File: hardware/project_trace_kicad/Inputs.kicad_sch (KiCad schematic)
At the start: 41 parts, among them J201 Conn_01x01_Socket, J202 Conn_01x01_Socket, J203 Conn_01x01_Socket, J204 Screw_Terminal_01x04, J205 Conn_Coaxial, U1 OPA2837IRUNT, U2 OPA2837IRUNT, U202 AQW280SX, U203 AQW282SX, U204 TS5A23159DGS, U206 TLE2426xLP

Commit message: Fix Footprints, Add ADC Footpring, begin Layout
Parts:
- U1, U2: footprint (none) -> ProjectTraceFootprints:OPA2837IRUNT; DigikeyPN (none) -> 296-53042-1-ND
- U204: footprint Package_SO:VSSOP-10_3x3mm_P0.5mm -> ProjectTraceFootprints:SOIC-10 - DGS0010A
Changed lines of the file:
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@@
 			)
 		)
-		(property "Footprint" "Package_SO:VSSOP-10_3x3mm_P0.5mm"
+		(property "Footprint" "ProjectTraceFootprints:SOIC-10 - DGS0010A"
 			(at 196.85 95.885 0)
 			(hide yes)
@@
 			)
 		)
-		(property "Footprint" ""
+		(property "Footprint" "ProjectTraceFootprints:OPA2837IRUNT"
 			(at 157.48 142.24 0)
 			(hide yes)
@@
 			)
 		)
+		(property "DigikeyPN" "296-53042-1-ND"
+			(at 157.48 142.24 0)
+			(hide yes)
+			(show_name no)
+			(do_not_autoplace no)
+			(effects
+				(font
+					(size 1.27 1.27)
+				)
+			)
+		)
 		(pin "10"
 		)
@@
 			)
 		)
-		(property "Footprint" ""
+		(property "Footprint" "ProjectTraceFootprints:OPA2837IRUNT"
 			(at 123.19 63.5 0)
 			(hide yes)
@@
 			)
 		)
+		(property "DigikeyPN" "296-53042-1-ND"
+			(at 123.19 63.5 0)
+			(hide yes)
+			(show_name no)
+			(do_not_autoplace no)
+			(effects
+				(font
+					(size 1.27 1.27)
+				)
+			)
+		)
 		(pin "6"
 		)
@@
 			)
 		)
-		(property "Footprint" ""
+		(property "Footprint" "ProjectTraceFootprints:OPA2837IRUNT"
 			(at 123.19 36.83 0)
 			(hide yes)
@@
 			)
 		)
+		(property "DigikeyPN" "296-53042-1-ND"
+			(at 123.19 36.83 0)
+			(hide yes)
+			(show_name no)
+			(do_not_autoplace no)
+			(effects
+				(font
+					(size 1.27 1.27)
+				)
+			)
+		)
 		(pin "6"
 		)
@@
 			)
 		)
-		(property "Footprint" ""
+		(property "Footprint" "ProjectTraceFootprints:OPA2837IRUNT"
 			(at 245.11 66.04 0)
 			(hide yes)
@@
 			)
 		)
+		(property "DigikeyPN" "296-53042-1-ND"
+			(at 245.11 66.04 0)
+			(hide yes)
+			(show_name no)
+			(do_not_autoplace no)
+			(effects
+				(font
+					(size 1.27 1.27)
+				)
+			)
+		)
 		(pin "10"
 		)
@@
 			)
 		)
-		(property "Footprint" "Package_SO:VSSOP-10_3x3mm_P0.5mm"
+		(property "Footprint" "ProjectTraceFootprints:SOIC-10 - DGS0010A"
 			(at 158.75 73.025 0)
 			(hide yes)
@@
 			)
 		)
-		(property "Footprint" ""
+		(property "Footprint" "ProjectTraceFootprints:OPA2837IRUNT"
 			(at 189.23 63.5 0)
 			(hide yes)
@@
 			)
 		)
+		(property "DigikeyPN" "296-53042-1-ND"
+			(at 189.23 63.5 0)
+			(hide yes)
+			(show_name no)
+			(do_not_autoplace no)
+			(effects
+				(font
+					(size 1.27 1.27)
+				)
+			)
+		)
 		(pin "10"
 		)
@@
 			)
 		)
-		(property "Footprint" "Package_SO:VSSOP-10_3x3mm_P0.5mm"
+		(property "Footprint" "ProjectTraceFootprints:SOIC-10 - DGS0010A"
 			(at 252.73 158.115 0)
 			(hide yes)
@@
 			)
 		)
-		(property "Footprint" ""
+		(property "Footprint" "ProjectTraceFootprints:OPA2837IRUNT"
 			(at 191.77 142.24 0)
 			(hide yes)
@@
 			(at 191.77 142.24 0)
 			(hide yes)
+			(show_name no)
+			(do_not_autoplace no)
+			(effects
+				(font
+					(size 1.27 1.27)
+				)
+			)
+		)
+		(property "DigikeyPN" "296-53042-1-ND"
+			(at 191.77 142.24 0)
+			(hide yes)

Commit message: Update Inputs.kicad_sch
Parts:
- U1, U2: footprint ProjectTraceFootprints:OPA2837IRUNT -> ProjectTraceFootprints:OPA2837IRUNT-Handsolder
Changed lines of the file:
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@@
 			)
 		)
-		(property "Footprint" "ProjectTraceFootprints:OPA2837IRUNT"
+		(property "Footprint" "ProjectTraceFootprints:OPA2837IRUNT-Handsolder"
 			(at 157.48 142.24 0)
 			(hide yes)
@@
 			)
 		)
-		(property "Footprint" "ProjectTraceFootprints:OPA2837IRUNT"
+		(property "Footprint" "ProjectTraceFootprints:OPA2837IRUNT-Handsolder"
 			(at 123.19 63.5 0)
 			(hide yes)
@@
 			)
 		)
-		(property "Footprint" "ProjectTraceFootprints:OPA2837IRUNT"
+		(property "Footprint" "ProjectTraceFootprints:OPA2837IRUNT-Handsolder"
 			(at 123.19 36.83 0)
 			(hide yes)
@@
 			)
 		)
-		(property "Footprint" "ProjectTraceFootprints:OPA2837IRUNT"
+		(property "Footprint" "ProjectTraceFootprints:OPA2837IRUNT-Handsolder"
 			(at 245.11 66.04 0)
 			(hide yes)
@@
 			)
 		)
-		(property "Footprint" "ProjectTraceFootprints:OPA2837IRUNT"
+		(property "Footprint" "ProjectTraceFootprints:OPA2837IRUNT-Handsolder"
 			(at 189.23 63.5 0)
 			(hide yes)
@@
 			)
 		)
-		(property "Footprint" "ProjectTraceFootprints:OPA2837IRUNT"
+		(property "Footprint" "ProjectTraceFootprints:OPA2837IRUNT-Handsolder"
 			(at 191.77 142.24 0)
 			(hide yes)

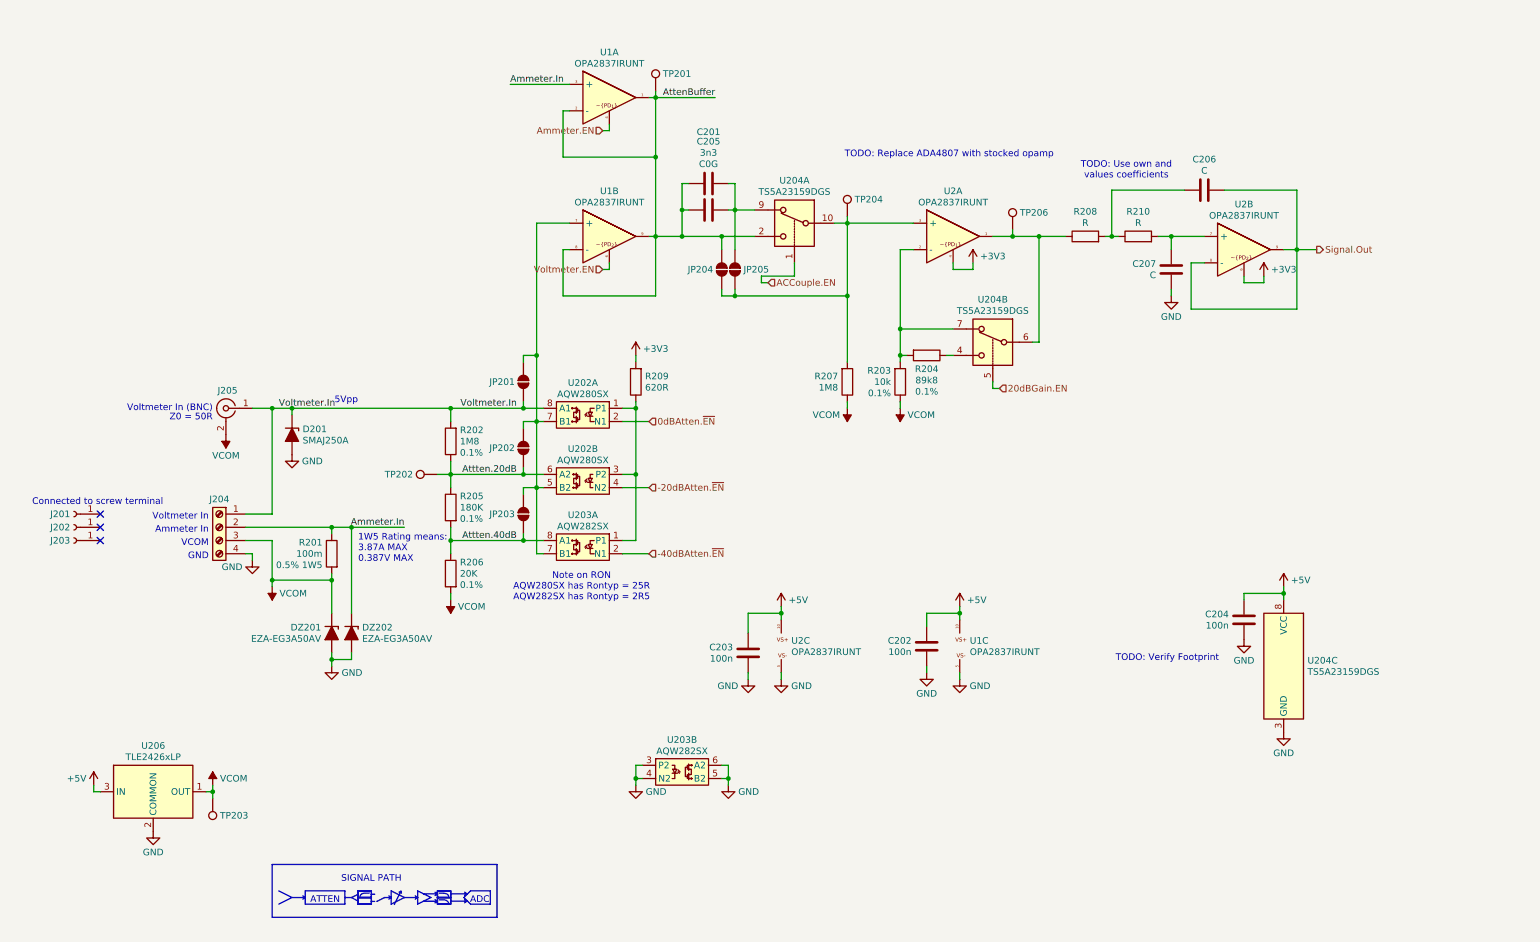
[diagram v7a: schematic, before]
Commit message: Implement AAAF, reintroduce differential driver.
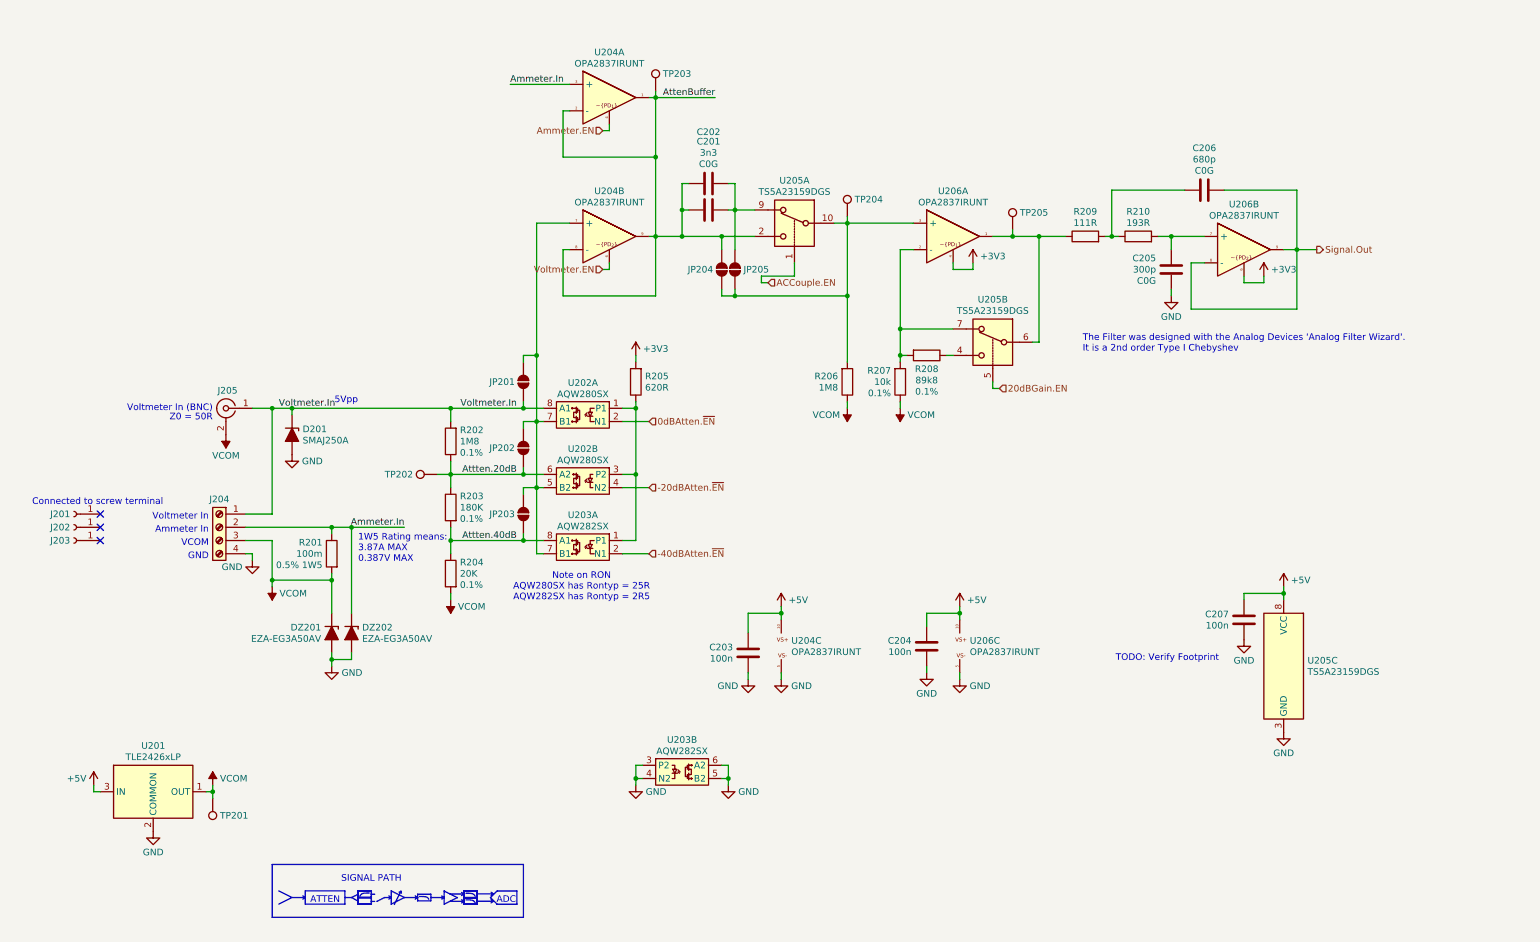
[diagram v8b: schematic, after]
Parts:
- C205: renamed from C207; value C -> 300p; footprint (none) -> Capacitor_SMD:C_0603_1608Metric_Pad1.08x0.95mm_HandSolder; Extra (none) -> C0G
- C206: value C -> 680p; footprint (none) -> Capacitor_SMD:C_0603_1608Metric_Pad1.08x0.95mm_HandSolder; Extra (none) -> C0G
- R209: renamed from R208; value R -> 111R; footprint (none) -> Resistor_SMD:R_0603_1608Metric_Pad0.98x0.95mm_HandSolder
- R210: value R -> 193R; footprint (none) -> Resistor_SMD:R_0603_1608Metric_Pad0.98x0.95mm_HandSolder
- renumbered C205 to C201, C201 to C202, C202 to C204, C204 to C207, R205 to R203, R206 to R204, R209 to R205, R207 to R206, R203 to R207, R204 to R208, TP203 to TP201, TP201 to TP203, TP206 to TP205, U206 to U201, U2 to U204, U1 to U204, U204 to U205, U2 to U206, U1 to U206
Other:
- note added: "The Filter was designed with the Analog Devices 'Analog Filter Wizard'. It is a 2nd order Type I Chebyshev"
- note removed: "TODO: Replace ADA4807 with stocked opamp"
- note removed: "TODO: Use own and values coefficients"
